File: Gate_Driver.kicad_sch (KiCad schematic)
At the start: 27 parts, among them U1 DRV8323RSRGZR

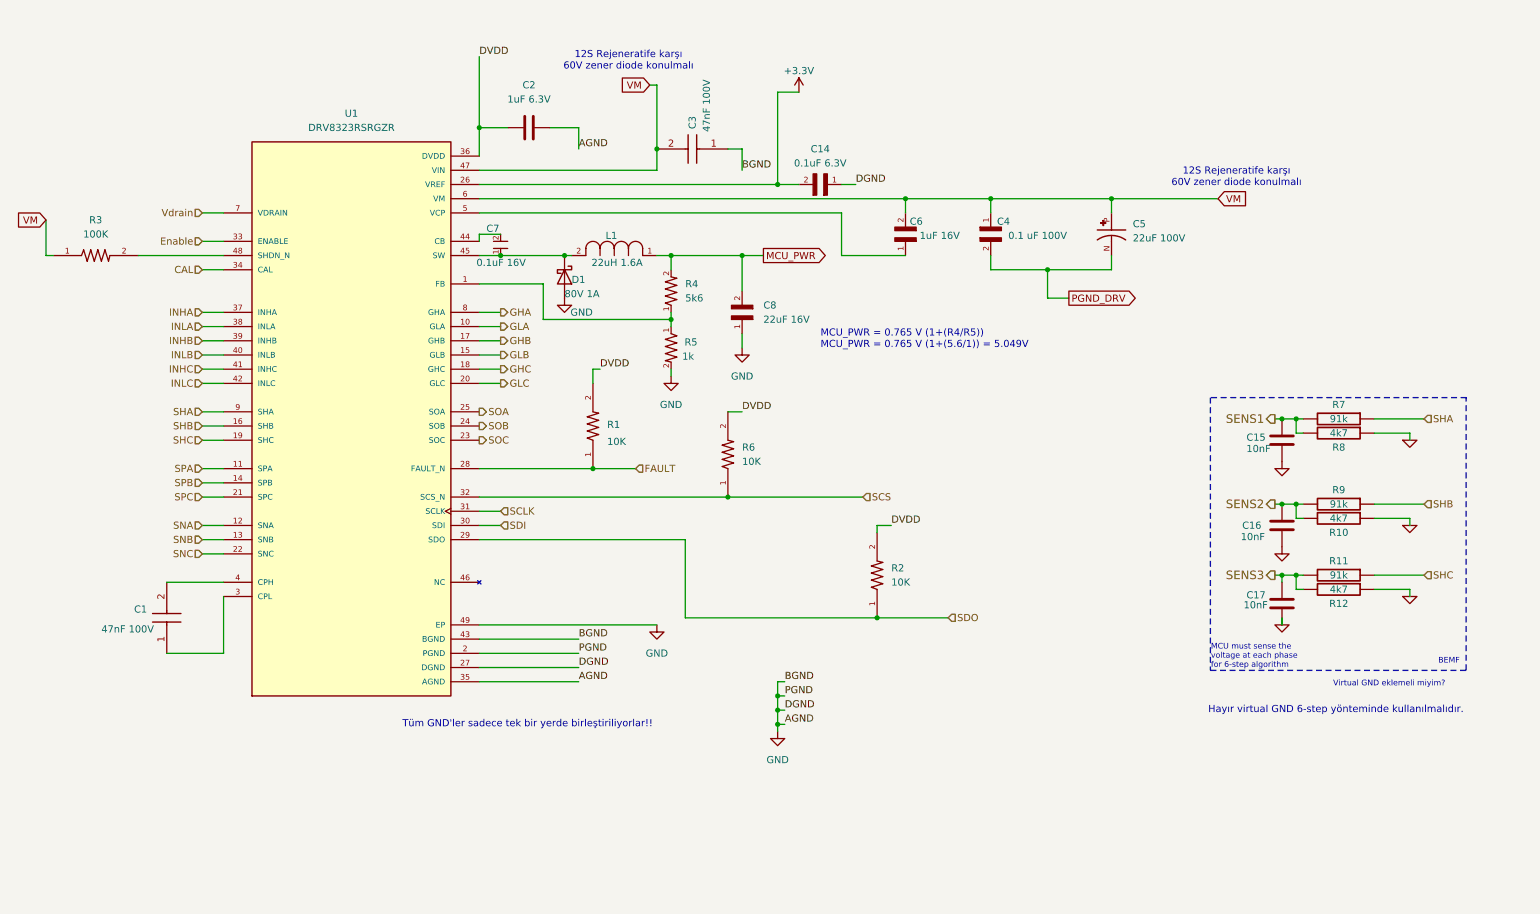
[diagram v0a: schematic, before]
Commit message: fixing design errors
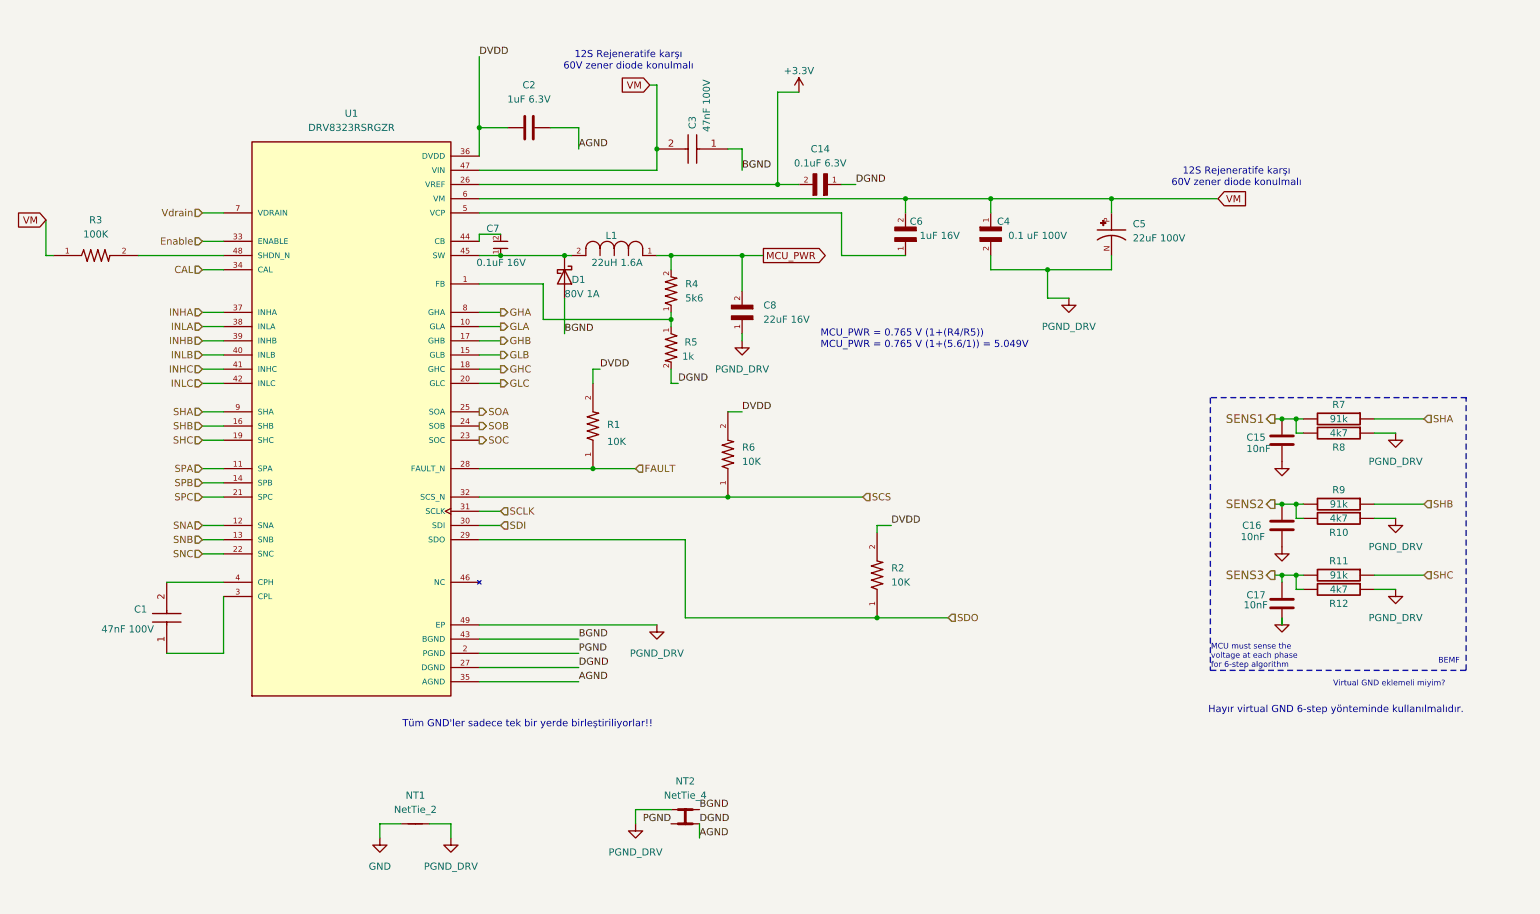
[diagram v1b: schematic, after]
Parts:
- added NT1: NetTie_2, symbol Device:NetTie_2
- added NT2: NetTie_4, NetTie:NetTie-4_SMD_Pad0.5mm, symbol Device:NetTie_4
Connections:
- net GND: now also NT1.1; no longer C14.1, C2.2, C3.1, C8.1, D1.2 (A), R10.1, R12.1, R5.2, R8.1, U1.2 (PGND), U1.27 (DGND), U1.35 (AGND), U1.43 (BGND), U1.49 (EP)
- net PGND_DRV: now also C8.1, R10.1, R12.1, R8.1, U1.49 (EP), NT1.2, NT2.1
- new net AGND: C14.1, C2.2, NT2.4, R5.2, U1.27 (DGND), U1.35 (AGND)
- new net BGND: C3.1, D1.2 (A), NT2.2, U1.43 (BGND)
- new net PGND: NT2.3, U1.2 (PGND)

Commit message: New one_GND_Layer pcb desgin has finished yet. DRC Rule checks needs to be controlling and correcting still.
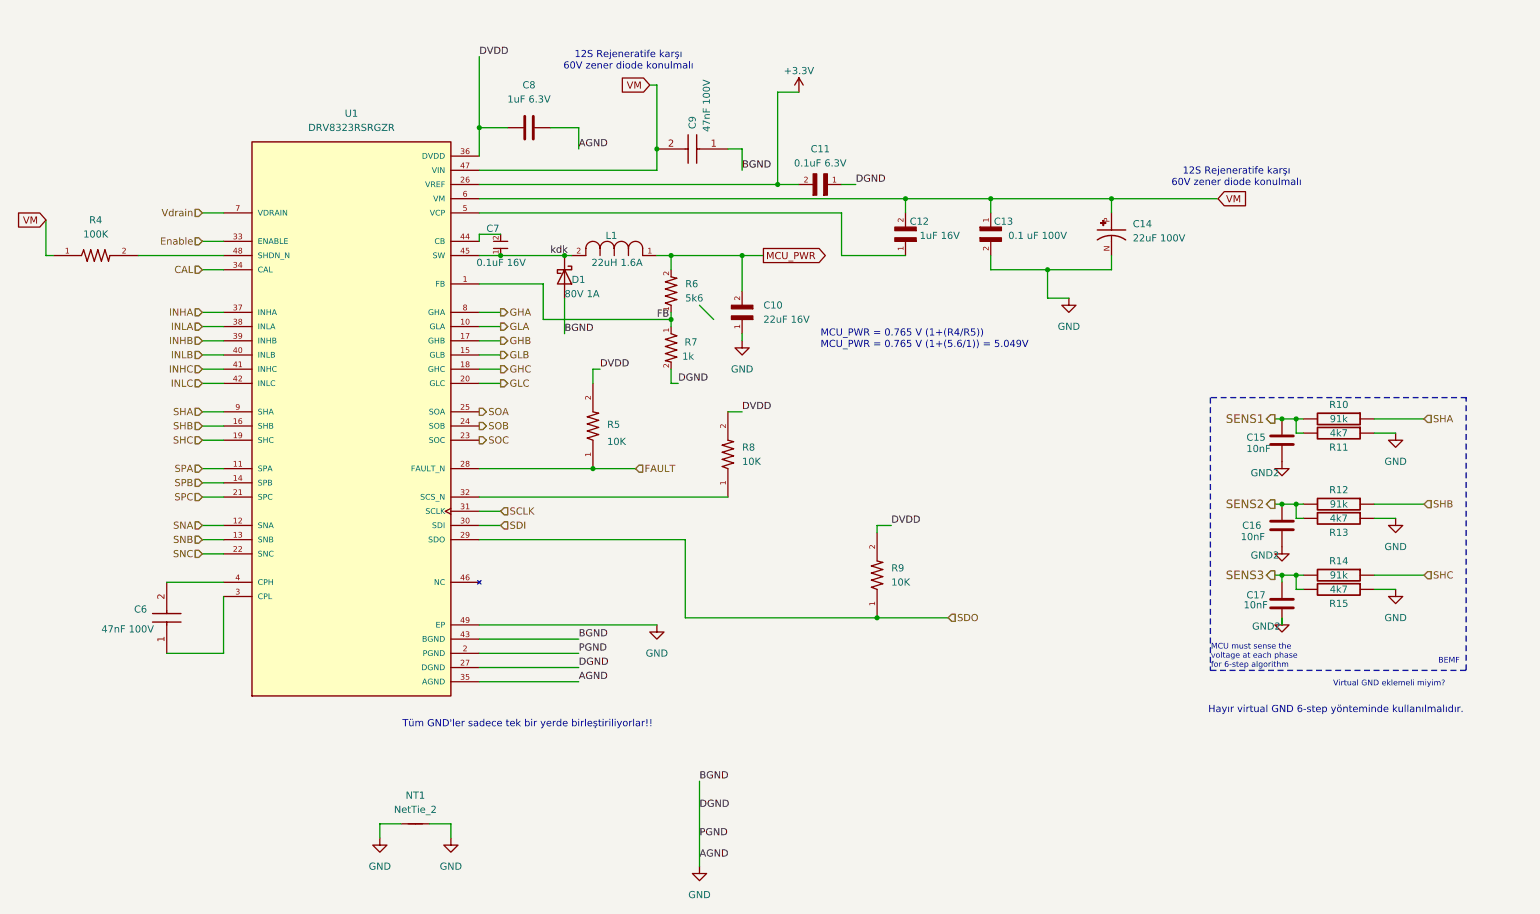
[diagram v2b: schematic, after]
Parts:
- removed NT2: NetTie_4, NetTie:NetTie-4_SMD_Pad0.5mm, symbol Device:NetTie_4
- renumbered C8 to C10, C14 to C11, C6 to C12, C4 to C13, C5 to C14, C1 to C6, C2 to C8, C3 to C9, R7 to R10, R8 to R11, R9 to R12, R10 to R13, R11 to R14, R12 to R15, R3 to R4, R1 to R5, R4 to R6, R5 to R7, R6 to R8, R2 to R9
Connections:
- net AGND is gone; now on net GND: C11.1, C8.2, R7.2, U1.27 (DGND), U1.35 (AGND)
- net BGND is gone; now on net GND: C9.1, D1.2 (A), U1.43 (BGND)
- net PGND is gone; now on net GND: U1.2 (PGND)
- net PGND_DRV is gone; now on net GND: C10.1, C13.2, C14.N, NT1.2, R11.1, R13.1, R15.1, U1.49 (EP)
- net GND: no longer C15.2, C16.2, C17.2
- net kdk: now reaches C7.1, D1.1 (K), L1.2, U1.45 (SW)
- net FB: now reaches R6.1, R7.1, U1.1 (FB)
- net SCS: no longer names the net of R8.1, U1.32 (SCS_N)
- new net GND2: C15.2, C16.2, C17.2

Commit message: minor rule checking warning
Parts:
- removed NT1: NetTie_2, symbol Device:NetTie_2
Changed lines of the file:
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@@
 	(wire
 		(pts
-			(xy 83.82 161.29) (xy 80.01 161.29)
-		)
-		(stroke
-			(width 0)
-			(type default)
-		)
-	)
-	(wire
-		(pts
 			(xy 243.84 88.9) (xy 245.11 88.9)
 		)
@@
 	(wire
 		(pts
-			(xy 80.01 161.29) (xy 80.01 163.83)
-		)
-		(stroke
-			(width 0)
-			(type default)
-		)
-	)
-	(wire
-		(pts
 			(xy 173.99 52.07) (xy 173.99 49.53)
 		)
@@
 	(wire
 		(pts
-			(xy 88.9 161.29) (xy 92.71 161.29)
-		)
-		(stroke
-			(width 0)
-			(type default)
-		)
-	)
-	(wire
-		(pts
 			(xy 101.6 55.88) (xy 97.79 55.88)
 		)
@@
 	(wire
 		(pts
-			(xy 92.71 161.29) (xy 92.71 163.83)
-		)
-		(stroke
-			(width 0)
-			(type default)
-		)
-	)
-	(wire
-		(pts
 			(xy 110.49 36.83) (xy 115.57 36.83)
 		)
@@
 	(symbol
 		(lib_id "power:GND")
-		(at 80.01 163.83 0)
-		(unit 1)
-		(exclude_from_sim no)
-		(in_bom yes)
-		(on_board yes)
-		(dnp no)
-		(fields_autoplaced yes)
-		(property "Reference" "#PWR09"
-			(at 80.01 170.18 0)
-			(effects
-				(font
-					(size 1.27 1.27)
-				)
-				(hide yes)
-			)
-		)
-		(property "Value" "GND"
-			(at 80.01 168.91 0)
-			(effects
-				(font
-					(size 1.27 1.27)
-				)
-			)
-		)
-		(property "Footprint" ""
-			(at 80.01 163.83 0)
-			(effects
-				(font
-					(size 1.27 1.27)
-				)
-				(hide yes)
-			)
-		)
-		(property "Datasheet" ""
-			(at 80.01 163.83 0)
-			(effects
-				(font
-					(size 1.27 1.27)
-				)
-				(hide yes)
-			)
-		)
-		(property "Description" "Power symbol creates a global label with name \"GND\" , ground"
-			(at 80.01 163.83 0)
-			(effects
-				(font
-					(size 1.27 1.27)
-				)
-				(hide yes)
-			)
-		)
-		(pin "1"
-		)
-		(instances
-			(project "Ana_ESC"
-				(path "/57129761-6d47-486c-bd7a-90dbb6f75754/beeab9ba-c868-48bf-b621-5886b9552033"
-					(reference "#PWR09")
-					(unit 1)
-				)
-			)
-		)
-	)
-	(symbol
-		(lib_id "power:GND")
 		(at 241.3 124.46 0)
 		(unit 1)
@@
 	)
 	(symbol
-		(lib_id "Device:NetTie_2")
-		(at 86.36 161.29 0)
-		(unit 1)
-		(exclude_from_sim no)
-		(in_bom no)
-		(on_board yes)
-		(dnp no)
-		(fields_autoplaced yes)
-		(property "Reference" "NT1"
-			(at 86.36 156.21 0)
-			(effects
-				(font
-					(size 1.27 1.27)
-				)
-			)
-		)
-		(property "Value" "NetTie_2"
-			(at 86.36 158.75 0)
-			(effects
-				(font
-					(size 1.27 1.27)
-				)
-			)
-		)
-		(property "Footprint" ""
-			(at 86.36 161.29 0)
-			(effects
-				(font
-					(size 1.27 1.27)
-				)
-				(hide yes)
-			)
-		)
-		(property "Datasheet" "~"
-			(at 86.36 161.29 0)
-			(effects
-				(font
-					(size 1.27 1.27)
-				)
-				(hide yes)
-			)
-		)
-		(property "Description" "Net tie, 2 pins"
-			(at 86.36 161.29 0)
-			(effects
-				(font
-					(size 1.27 1.27)
-				)
-				(hide yes)
-			)
-		)
-		(pin "1"
-		)
-		(pin "2"
-		)
-		(instances
-			(project ""
-				(path "/57129761-6d47-486c-bd7a-90dbb6f75754/beeab9ba-c868-48bf-b621-5886b9552033"
-					(reference "NT1")
-					(unit 1)
-				)
-			)
-		)
-	)
-	(symbol
 		(lib_id "DRV8323RSRGZR:DRV8323RSRGZR")
 		(at 74.93 87.63 0)
@@
 					(unit 1)
 				)
-			)
-		)
-	)
-	(symbol
-		(lib_id "power:GND")
-		(at 92.71 163.83 0)
-		(unit 1)
-		(exclude_from_sim no)
-		(in_bom yes)
-		(on_board yes)
-		(dnp no)
-		(fields_autoplaced yes)
-		(property "Reference" "#PWR010"
-			(at 92.71 170.18 0)
-			(effects
-				(font
-					(size 1.27 1.27)
-				)
-				(hide yes)
-			)
-		)
-		(property "Value" "GND"
-			(at 92.71 168.91 0)
-			(effects
-				(font
-					(size 1.27 1.27)
-				)
-			)
-		)
-		(property "Footprint" ""
-			(at 92.71 163.83 0)
-			(effects
-				(font
-					(size 1.27 1.27)
-				)
-				(hide yes)
-			)
-		)
-		(property "Datasheet" ""
-			(at 92.71 163.83 0)
-			(effects
-				(font
-					(size 1.27 1.27)
-				)
-				(hide yes)
-			)
-		)
-		(property "Description" "Power symbol creates a global label with name \"GND\" , ground"
-			(at 92.71 163.83 0)
-			(effects
-				(font
-					(size 1.27 1.27)
-				)
-				(hide yes)
-			)
-		)
-		(pin "1"
-		)
-		(instances
-			(project "Ana_ESC"
-				(path "/57129761-6d47-486c-bd7a-90dbb6f75754/beeab9ba-c868-48bf-b621-5886b9552033"
-					(reference "#PWR010")
-					(unit 1)
-				)

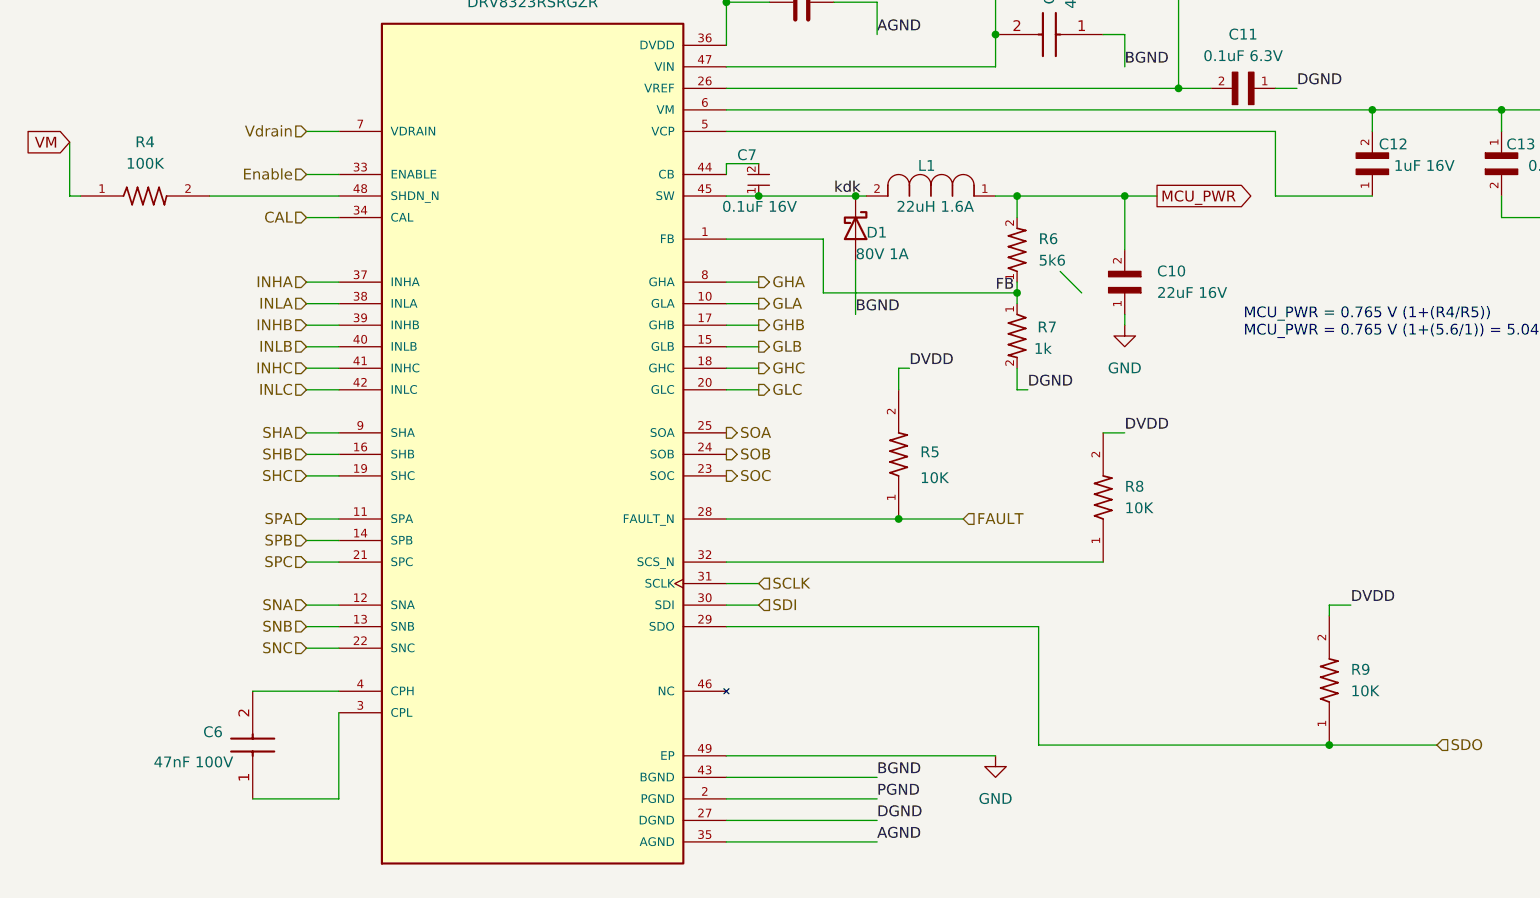
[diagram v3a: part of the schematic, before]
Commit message: BOM list prepared for ekom and direnc.net
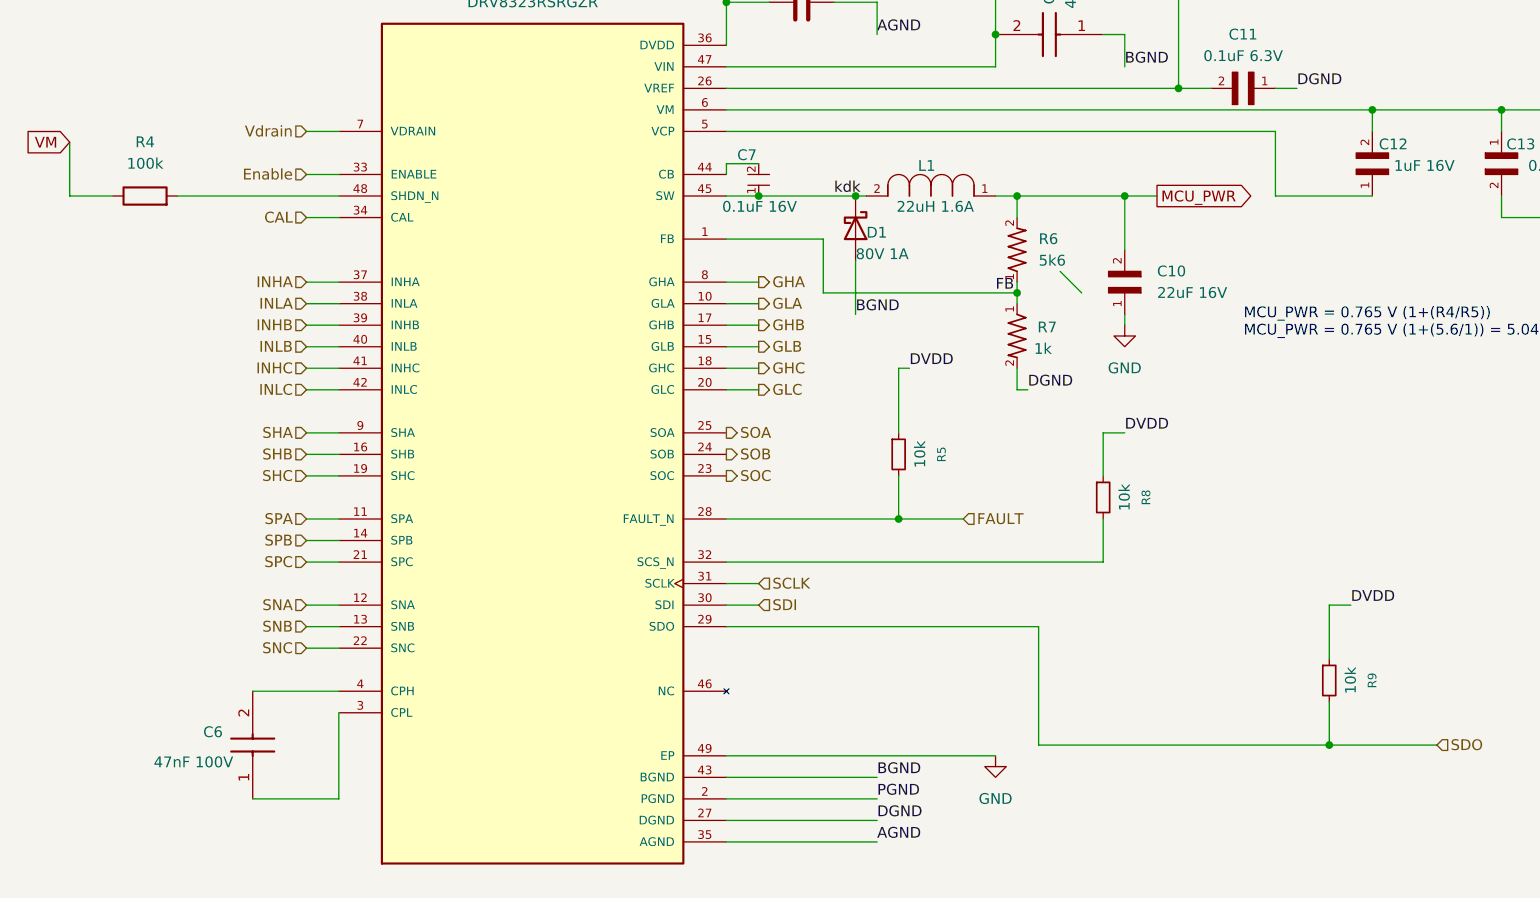
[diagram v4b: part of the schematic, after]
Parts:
- removed R4: 100K, RC0603FR-07100KL:RESC1607X60N, symbol RC0603FR-07100KL:RC0603FR-07100KL
- removed R5, R8, R9: 10K, RC0603FR-0710KL:RESC1607X60N, symbol RC0603FR-0710KL:RC0603FR-0710KL
- added R4: 100k, Resistor_SMD:R_0603_1608Metric_Pad0.98x0.95mm_HandSolder, symbol Device:R
- added R5, R8, R9: 10k, Resistor_SMD:R_0603_1608Metric_Pad0.98x0.95mm_HandSolder, symbol Device:R_Small
- R7: footprint RNCP0603FTD1K00:RESC1508X50N -> Resistor_SMD:R_0603_1608Metric_Pad0.98x0.95mm_HandSolder
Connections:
- net DVDD: now also R5.1, R8.1, R9.1
- net FAULT: now also R5.2
- net SDO: now also R9.2
- net VM: now also R4.1
- net at U1.48 (SHDN_N): now also R4.2
- net at U1.32 (SCS_N): now also R8.2
